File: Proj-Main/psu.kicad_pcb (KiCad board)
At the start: 2 copper layers, 100 x 75 mm, 111 parts, among them J1 METER, J3 T1A, J4 T1B, J5 T1C, J6 SENSE, J8 OUT+, J9 OUT-, Q1 MMBT3906, Q10 MMBT2907A, Q11 PMP4201Y, Q12 MMBT3904, Q13 MMBT2907A, Q14 MMBT3904, Q15 PZT2222A, Q16 MMBT3904, Q17 TIP105, Q18 PMP4201Y, Q19 MMBT2907A, Q2 MMBT3904, Q20 MMBT2907A, Q21 MMBT2907A, Q22 MMBT3904, Q3 PZT2222A, Q4 MMBT3906, Q5 MMBT3906, Q6 MMBT3906, Q7 PMP4201Y, Q8 PMP4201Y, Q9 MMBT2907A

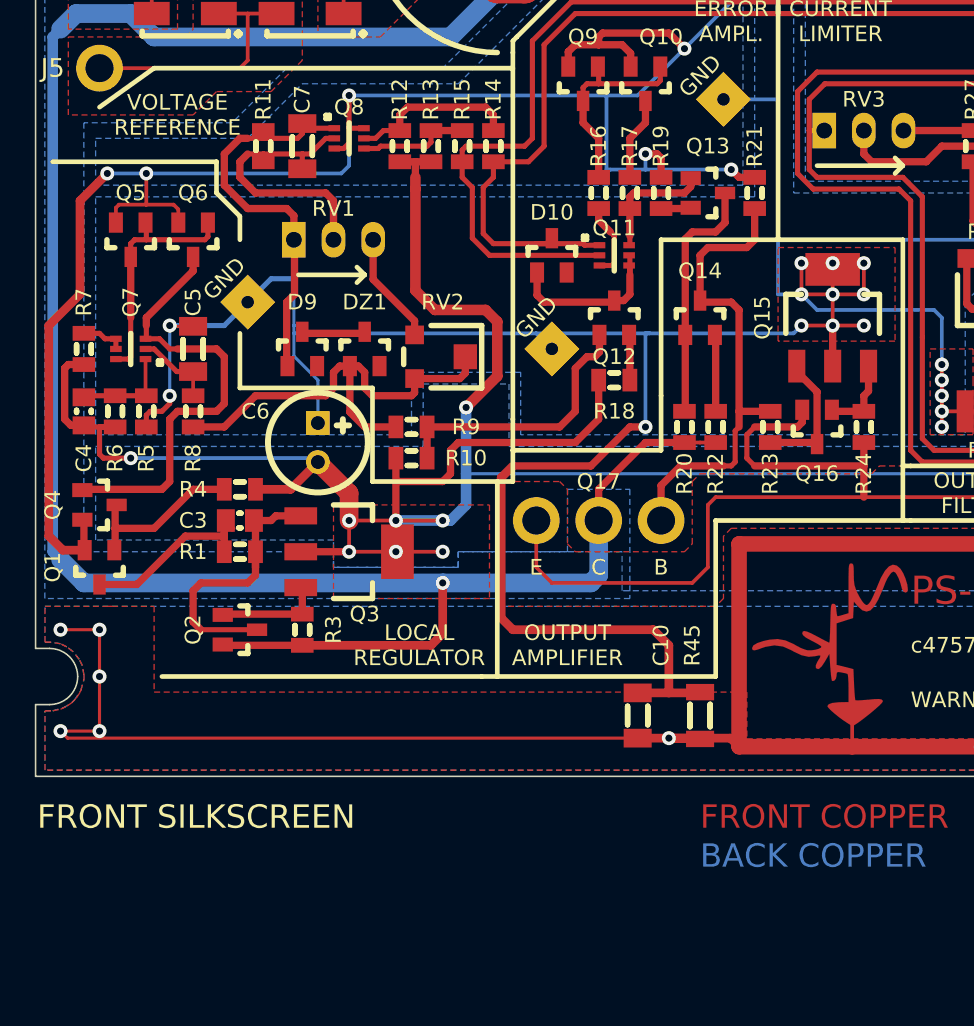
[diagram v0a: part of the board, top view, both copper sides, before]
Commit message: Added R46, R47
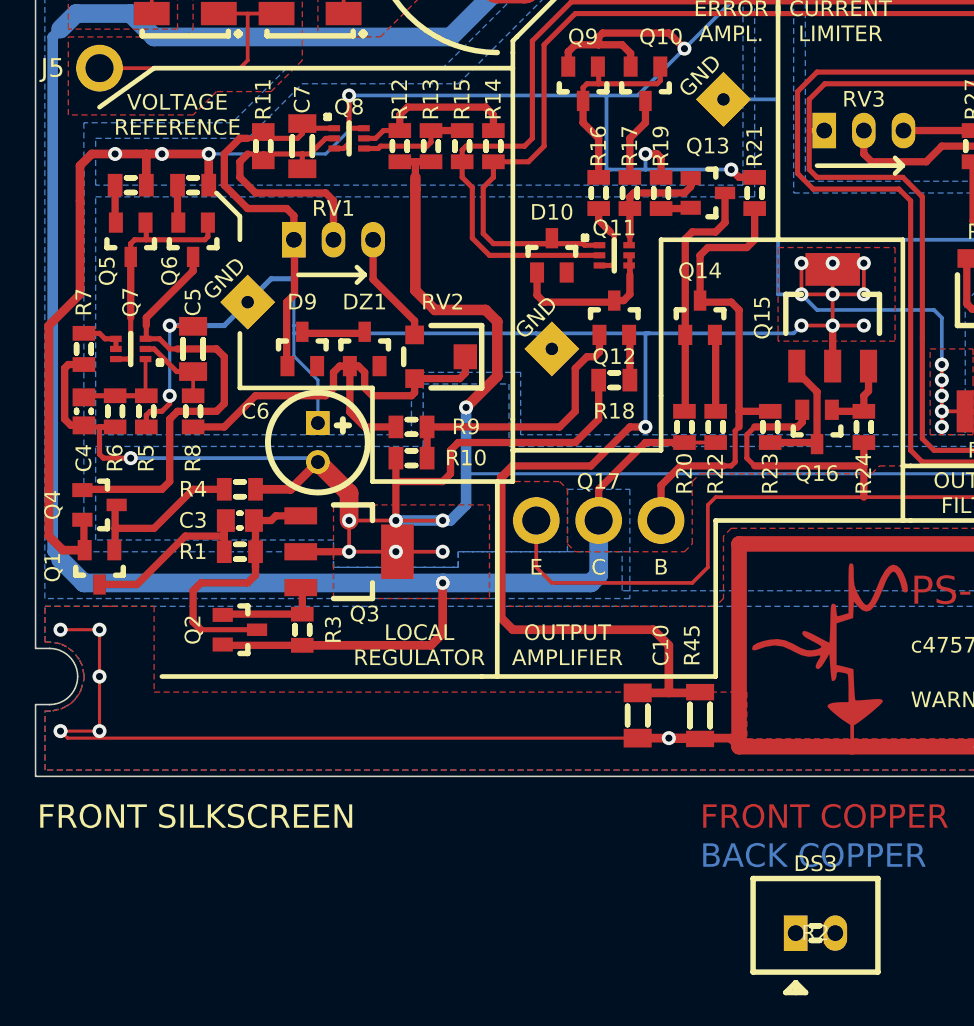
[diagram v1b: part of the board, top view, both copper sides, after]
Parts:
- added DS3: POWER, conn:CONN_2-SIL, F.Cu at (174.9, 142.5)
- added R2: 10k, IPC7351-Nominal:RESC2012X50, F.Cu at (174.9, 142.5)
- added R46: 1k, IPC7351-Nominal:RESC2012X50, F.Cu at (131.0, 94.5)
- added R47: 1k, IPC7351-Nominal:RESC2012X50, F.Cu at (135.0, 94.5)
- Q1, Q4: value MMBT3906 -> BC856
- R37, R38: value 120k 0.5% -> * 0.5%
- R39, R40: value 100 -> 270
- RV3: value 10k -> 1k
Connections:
- Q5 pad 2: V+ -> Net-(Q5-Pad2)
- Q6 pad 2: V+ -> Net-(Q6-Pad2)
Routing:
- net V+: track 252.6 -> 248.6 mm, vias 9 -> 10
- net Net-(Q6-Pad2): track 0.00 -> 2.42 mm
- net Net-(Q5-Pad2): track 0.00 -> 2.42 mm

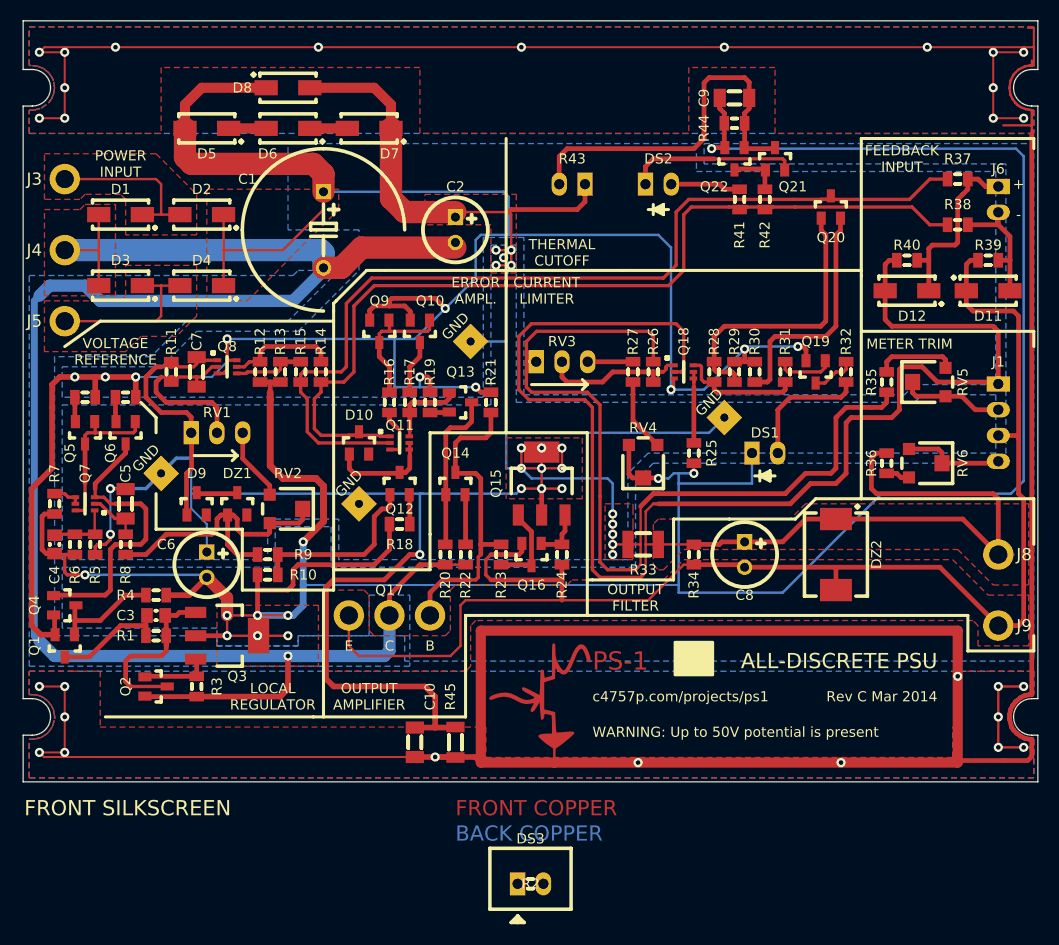
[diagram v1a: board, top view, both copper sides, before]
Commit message: Added power LED DS3
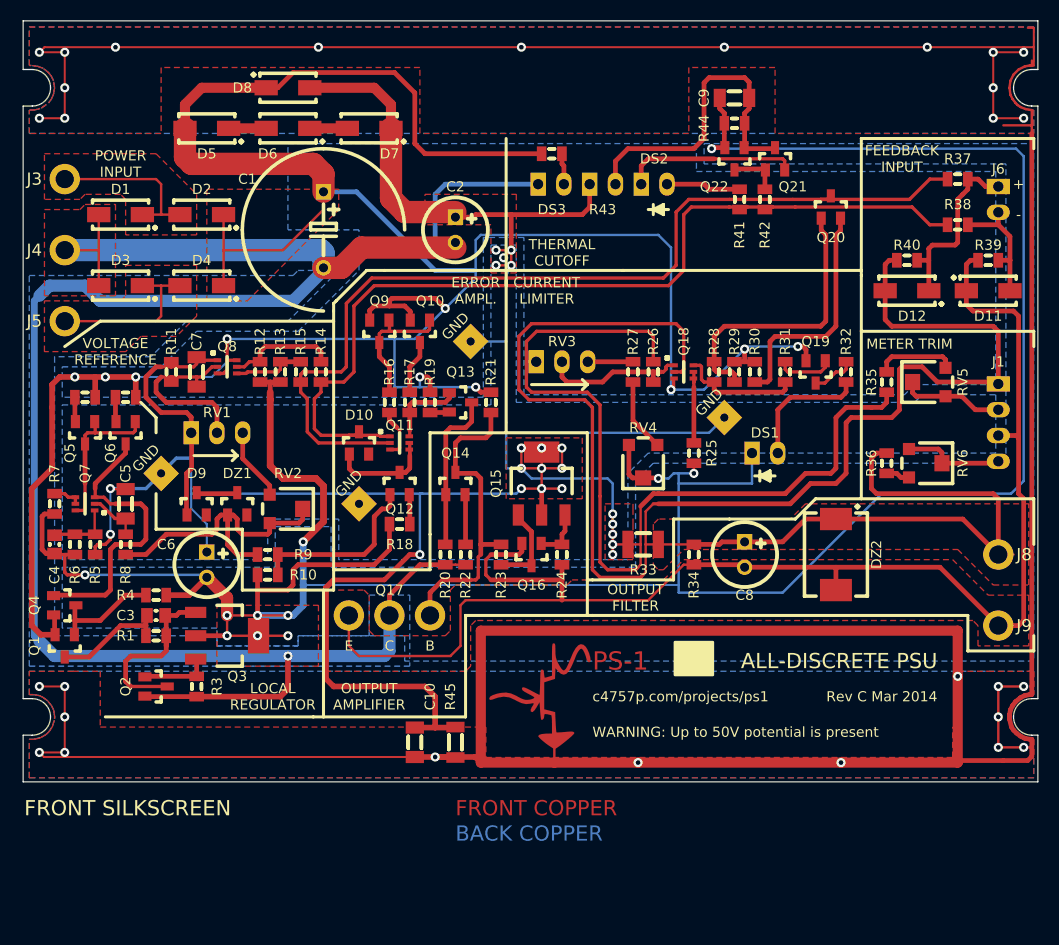
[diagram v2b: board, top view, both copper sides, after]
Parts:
- moved R2 72.0 mm to (177.0, 70.5)
- moved DS3 69.0 mm to (176.9, 73.5)
- moved R43 3.00 mm to (182.0, 73.5), turned to 0 degrees
- moved DS2 0.42 mm to (187.1, 73.5)
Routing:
- net V+: track 248.6 -> 278.0 mm
- net V-UNREG: track 183.5 -> 201.0 mm
- net Net-(C9-Pad1): track 37.9 -> 32.1 mm
- net Net-(DS3-PadA): track 0.00 -> 3.08 mm
- net GND: track 357.8 -> 358.4 mm

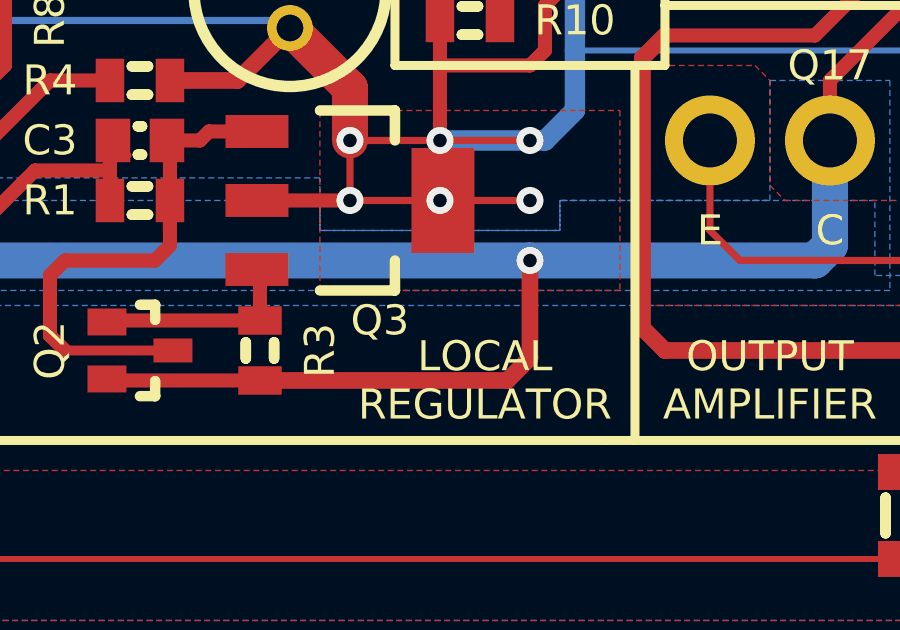
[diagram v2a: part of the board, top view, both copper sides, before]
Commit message: Added regulator bootstrap resistor R48
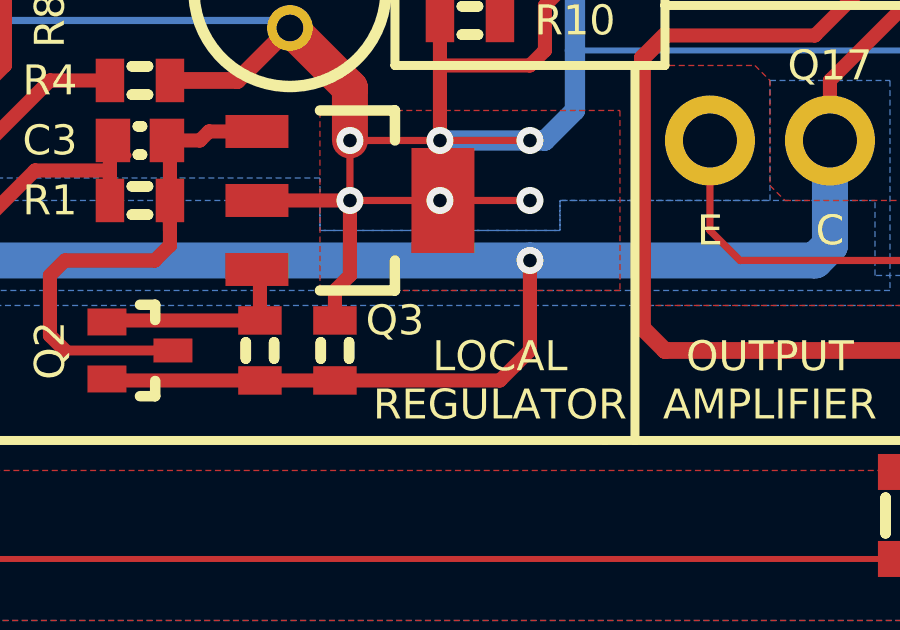
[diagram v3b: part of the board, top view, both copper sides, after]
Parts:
- added R48: 22k, IPC7351-Nominal:RESC2012X50, F.Cu at (144.5, 123.0)
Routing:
- net V-: track 287.5 -> 291.7 mm

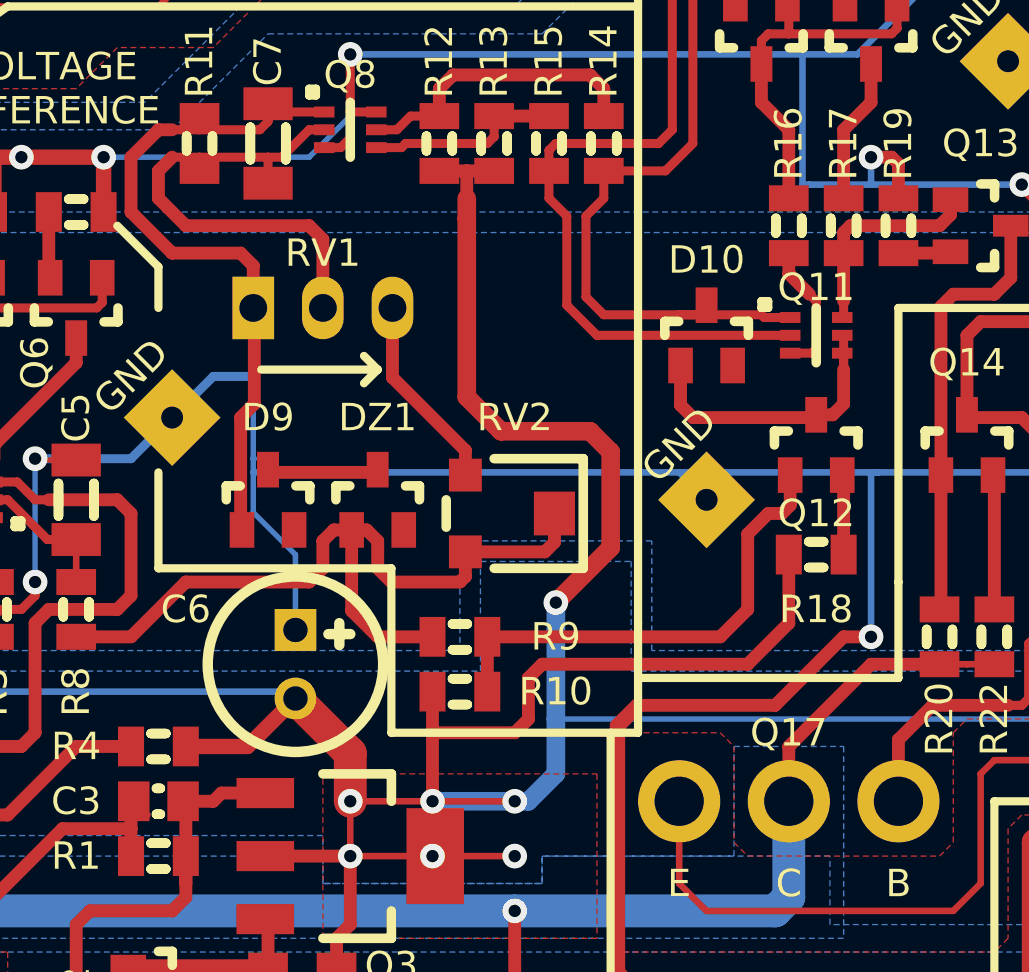
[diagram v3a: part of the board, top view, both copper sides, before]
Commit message: Improved design of current source
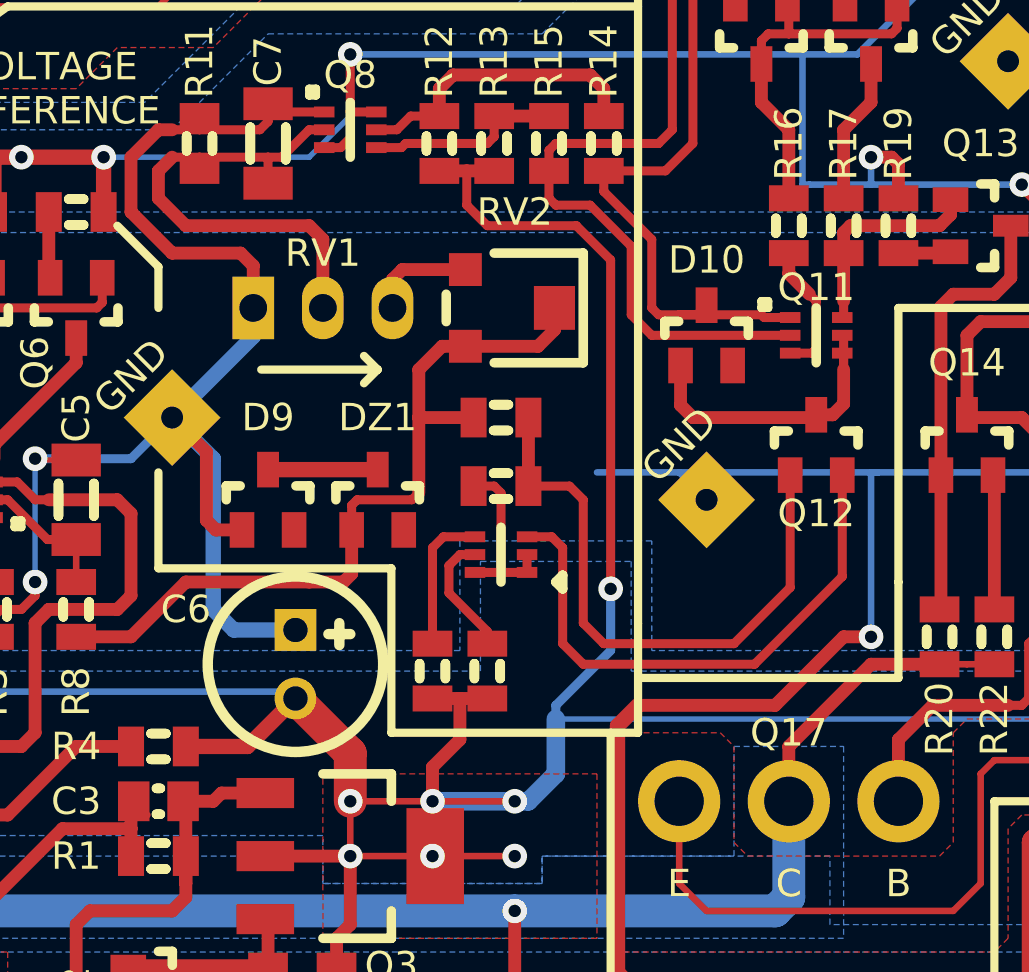
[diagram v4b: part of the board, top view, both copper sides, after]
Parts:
- added Q23: PMP4201Y, IPC-semi-nominal:SC-70-6, F.Cu at (150.5, 107.0)
- added R49: 33, IPC7351-Nominal:RESC2012X50, F.Cu at (148.0, 111.2)
- R18: value 1k -> 33
- R5: value 22k -> 30k
- R6: value 18k -> 22k
- moved R18 12.7 mm to (150.0, 111.2), turned to 270 degrees
- moved R9 8.14 mm to (150.5, 102.0)
- moved R10 7.65 mm to (150.5, 104.5)
- moved RV2 7.50 mm to (151.0, 98.0)
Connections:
- R10 pad 2: V- -> Net-(Q23-Pad1)
- R18 pad 1: Net-(Q12-Pad2) -> Net-(Q23-Pad5)
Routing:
- net Net-(Q12-Pad2): track 2.99 -> 20.6 mm
- net V-: track 291.7 -> 275.8 mm
- net GND: track 358.4 -> 343.4 mm
- net Net-(Q23-Pad1): track 0.00 -> 6.55 mm
- net Net-(Q23-Pad4): track 0.00 -> 5.22 mm
- net Net-(Q23-Pad5): track 0.00 -> 4.55 mm
- net Net-(Q12-Pad1): track 17.7 -> 22.0 mm
- net Net-(RV1-Pad3): track 7.20 -> 3.85 mm
- net /FB-: track 92.1 -> 90.4 mm
- net Net-(DZ1-Pad1): track 29.5 -> 29.0 mm

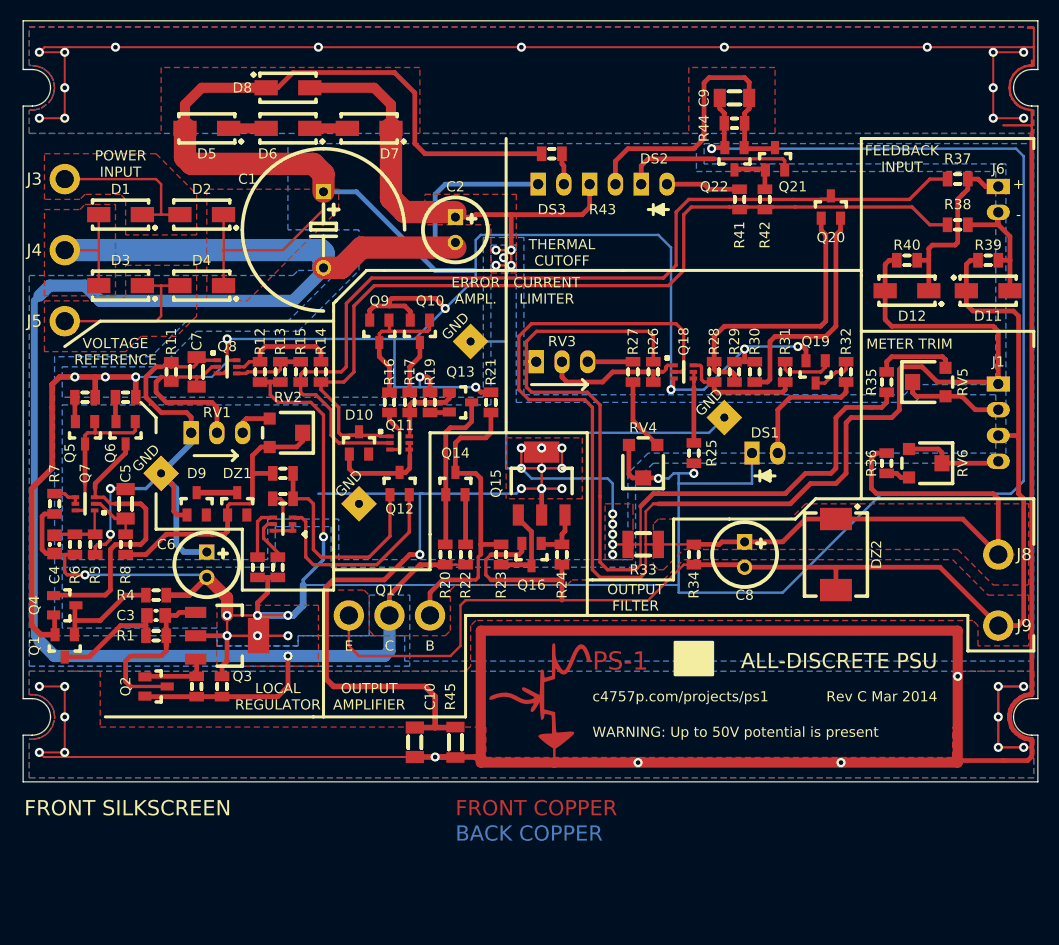
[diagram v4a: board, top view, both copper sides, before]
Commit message: Added new thermal cutoff
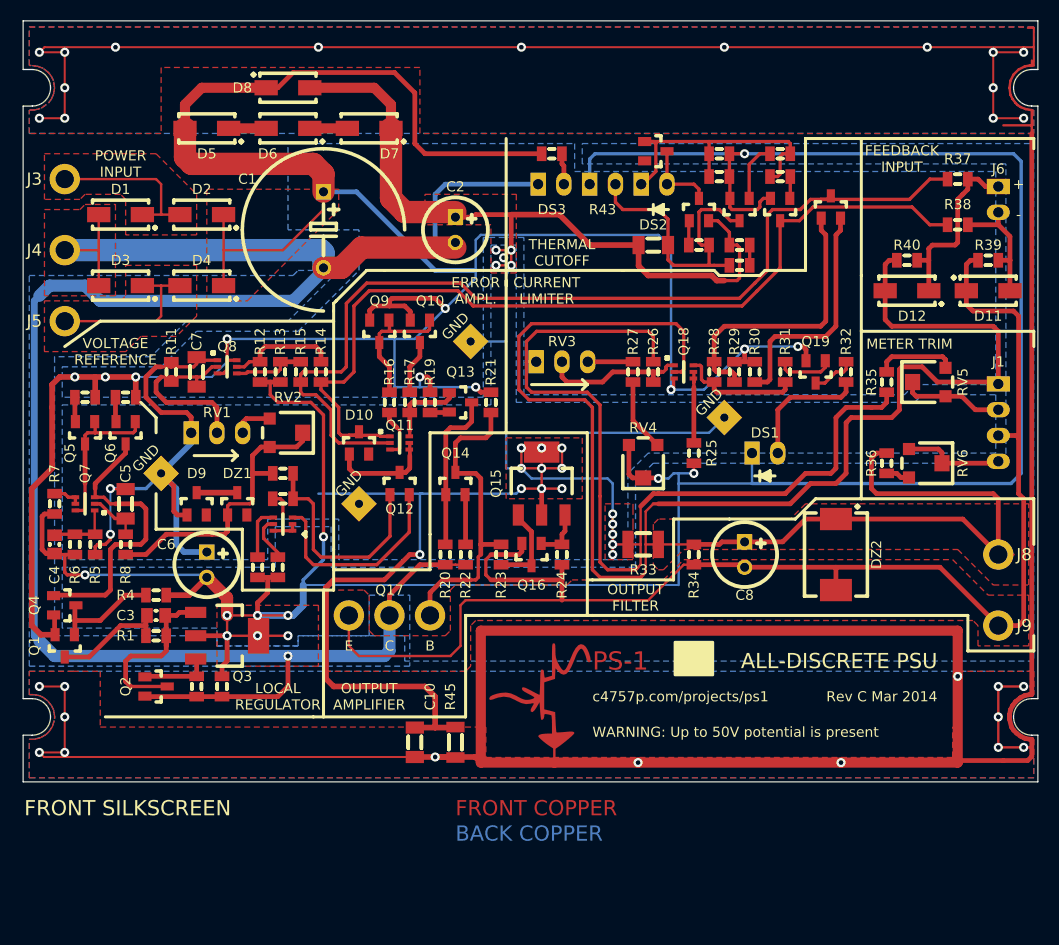
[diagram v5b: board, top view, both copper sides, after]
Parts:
- added DZ3: 3v0, IPC-semi-nominal:SOT-23, F.Cu at (187.2, 70.2)
- added Q24: MMBT3904, IPC-semi-nominal:SOT-23, F.Cu at (199.5, 76.0)
- added R50: 1k, IPC7351-Nominal:RESC2012X50, F.Cu at (195.5, 81.5)
- added R51: 10k, IPC7351-Nominal:RESC2012X50, F.Cu at (193.5, 70.5)
- added R52: 10k, IPC7351-Nominal:RESC2012X50, F.Cu at (193.5, 72.8)
- added R53: 10k, IPC7351-Nominal:RESC2012X50, F.Cu at (199.5, 72.8)
- Q10, Q13, Q9: value MMBT2907A -> BC856
- R42: value 100k -> 10k
- R43: value 100k -> NTC
- R44: value 270 -> 1k
- moved C9 16.6 mm to (187.0, 79.5), turned to 0 degrees
- moved R44 12.0 mm to (195.5, 79.5), turned to 0 degrees
- moved Q21 9.01 mm to (191.5, 76.0)
- moved R42 7.91 mm to (191.5, 79.5), turned to 0 degrees
- moved R41 6.02 mm to (199.5, 70.5), turned to 180 degrees
- moved Q22 5.02 mm to (195.5, 76.0)
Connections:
- C9 pad 1: Net-(C9-Pad1) -> GND
- C9 pad 2: V- -> Net-(C9-Pad2)
- Q21 pad 2: Net-(DS2-PadK) -> GND
- Q21 pad 3: Net-(C9-Pad1) -> Net-(DS2-PadA)
- Q22 pad 1: Net-(C9-Pad1) -> Net-(Q22-Pad1)
- Q22 pad 3: Net-(Q21-Pad1) -> Net-(C9-Pad2)
- R41 pad 1: /FB- -> Net-(DS2-PadK)
- R41 pad 2: Net-(DS2-PadA) -> Net-(Q22-Pad1)
- R42 pad 1: /FB- -> Net-(Q21-Pad1)
- R42 pad 2: Net-(Q21-Pad1) -> Net-(C9-Pad2)
- R43 pad 1: GND -> V-
- R43 pad 2: Net-(C9-Pad1) -> Net-(C9-Pad2)
- R44 pad 1: Net-(C9-Pad1) -> GND
- R44 pad 2: V- -> Net-(R44-Pad2)
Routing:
- net Net-(C9-Pad1): track 32.1 -> 0.00 mm
- net Net-(C9-Pad2): track 0.00 -> 28.7 mm
- net GND: track 343.4 -> 367.5 mm
- net Net-(DS2-PadK): track 17.2 -> 29.0 mm
- net V-: track 275.8 -> 282.0 mm
- net Net-(Q22-Pad1): track 0.00 -> 5.83 mm
- net Net-(Q21-Pad1): track 5.12 -> 2.42 mm
- net Net-(Q24-Pad1): track 0.00 -> 2.24 mm
- net Net-(R44-Pad2): track 0.00 -> 2.00 mm
- net /FB+: track 93.7 -> 95.1 mm
- net /FB-: track 90.4 -> 89.5 mm
